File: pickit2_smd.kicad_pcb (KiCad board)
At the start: 2 copper layers, 54 parts, among them CON1 USB-MINI-B, P1 CONN_6, Q1 MOSFET_P, Q2 MOSFET_N, Q3 MOSFET_P, Q4 MOSFET_N, Q5 MOSFET_N, Q6 MOSFET_P, Q7 MOSFET_N, Q8 20MHz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

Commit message: footprint certo pic
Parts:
- U2: footprint SOJ28_WIDE -> SO28
- moved U2 1.40 mm to (190.6, 135.1)
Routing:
- net /RB2: track 108.2 -> 100.5 mm
- net /RB4: track 100.3 -> 93.9 mm
- net /RB5: track 6.89 -> 9.55 mm
- net /RB3: track 39.3 -> 36.6 mm
- net +5V: track 120.6 -> 122.5 mm
- net GND: track 258.2 -> 260.0 mm
- net N-000004: track 31.8 -> 33.4 mm
- net N-000005: track 29.9 -> 31.6 mm
- net /D+: track 11.8 -> 13.1 mm
- net N-0000036: track 16.8 -> 15.9 mm
- net /D-: track 12.6 -> 13.1 mm
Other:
- rule via_min_size: 0.889 -> 1

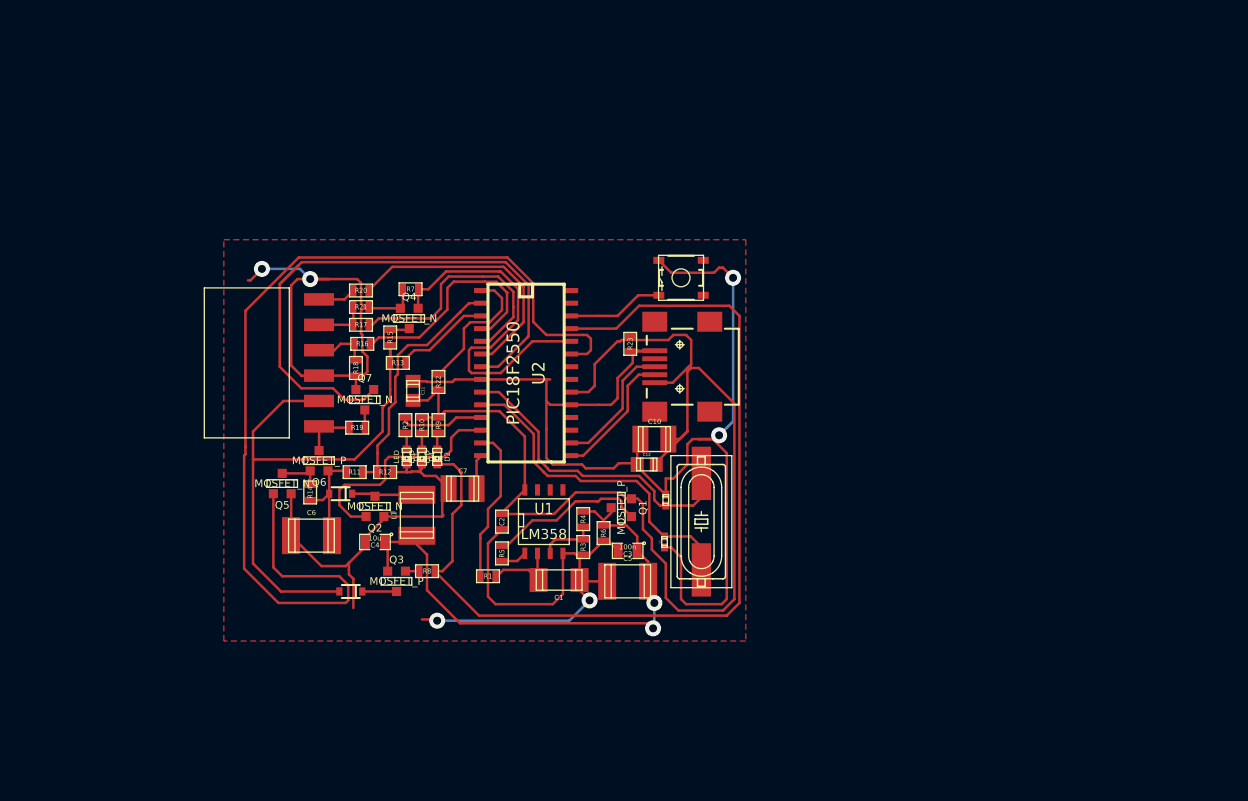
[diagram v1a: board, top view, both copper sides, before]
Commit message: versao modificada, PCB 50%
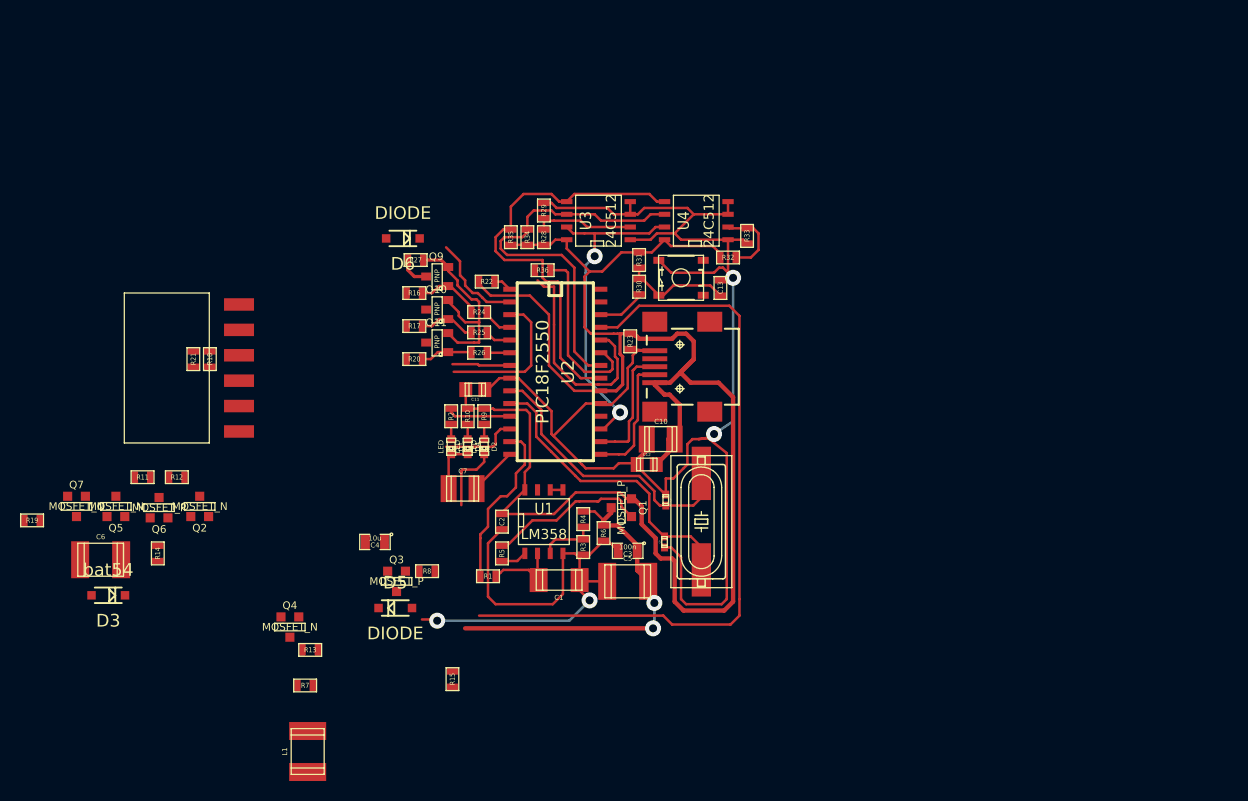
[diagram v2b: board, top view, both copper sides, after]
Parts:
- added C13: 100n, SM0603, F.Cu at (210.1, 126.6)
- added D6: DIODE, SOD123_mod, F.Cu at (178.3, 121.7)
- added Q10: PNP, SOT23, F.Cu at (181.7, 128.8)
- added Q11: PNP, SOT23, F.Cu at (181.7, 132.1)
- added Q9: PNP, SOT23, F.Cu at (181.7, 125.5)
- added R24: 33, SM0603, F.Cu at (185.9, 129.0)
- added R25: 33, SM0603, F.Cu at (185.9, 131.1)
- added R26: 33, SM0603, F.Cu at (185.9, 133.1)
- added R27: 820, SM0603, F.Cu at (179.6, 123.8)
- added R28: R, SM0603, F.Cu at (192.4, 121.5)
- added R29: R, SM0603, F.Cu at (192.4, 118.9)
- added R30: 33, SM0603, F.Cu at (201.9, 126.5)
- added R31: 10k, SM0603, F.Cu at (201.9, 123.8)
- added R32: R, SM0603, F.Cu at (210.8, 123.6)
- added R33: R, SM0603, F.Cu at (212.7, 121.4)
- added R34: R, SM0603, F.Cu at (190.8, 121.5)
- added R35: R, SM0603, F.Cu at (189.1, 121.5)
- added R36: 0, SM0603, F.Cu at (192.3, 124.8)
- added U3: 24C512, SO8N, F.Cu at (197.9, 119.9)
- added U4: 24C512, SO8N, F.Cu at (207.6, 119.9)
- D3: value DIODE -> bat54; footprint SparkFun-SOD-323 -> SOD123_mod
- D5: footprint SparkFun-SOD-323 -> SOD123_mod
- moved R7 41.0 mm to (168.5, 166.4)
- moved R15 34.7 mm to (183.3, 165.7)
- moved R19 33.8 mm to (141.2, 149.9)
- moved Q4 33.1 mm to (167.0, 160.5)
- moved Q7 30.7 mm to (145.7, 148.5)
- moved R13 30.0 mm to (169.0, 162.8)
- moved L1 26.0 mm to (168.8, 173.0)
- moved D3 25.4 mm to (148.8, 157.4)
- moved C6 21.2 mm to (148.1, 153.8)
- moved R11 21.2 mm to (152.3, 145.5)
- moved R12 20.8 mm to (155.7, 145.5)
- moved R21 17.6 mm to (157.4, 133.7), turned to 270 degrees
- moved Q2 17.5 mm to (158.0, 148.5)
- moved Q5 16.8 mm to (149.6, 148.5)
- moved Q6 16.7 mm to (153.9, 148.6)
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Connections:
- R16 pad 1: /RA2 -> N-0000011
- R17 pad 1: /RA3 -> N-0000014
- R20 pad 1: /RA4 -> N-0000017
- SW1 pad 1: /RB5 -> N-0000025
- U1 pad 5: (no net) -> GND
- U1 pad 6: (no net) -> GND
- U1 pad 7: (no net) -> N-0000018
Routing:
- net /RB2: track 100.5 -> 18.0 mm
- net N-0000033: track 55.3 -> 0.00 mm
- net /RA5: track 60.0 -> 5.77 mm
- net +5V: track 122.5 -> 170.5 mm
- net GND: track 260.0 -> 215.8 mm, vias 6 -> 4
- net /RB0: track 0.00 -> 43.5 mm
- net /RB1: track 0.00 -> 39.8 mm
- net /RC6: track 0.00 -> 32.6 mm, vias 0 -> 2
- net /RA4: track 26.4 -> 2.29 mm
- net /RA3: track 25.2 -> 2.60 mm
- net /RA2: track 23.3 -> 3.07 mm
- net /clamp: track 0.00 -> 19.7 mm
- net N-0000048: track 55.3 -> 37.9 mm
- net /RC1: track 23.2 -> 7.68 mm
- net /RB4: track 93.9 -> 78.8 mm
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- removed copper zone on F.Cu, net GND

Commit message: placa feita, falta a bobina e alargar pistas
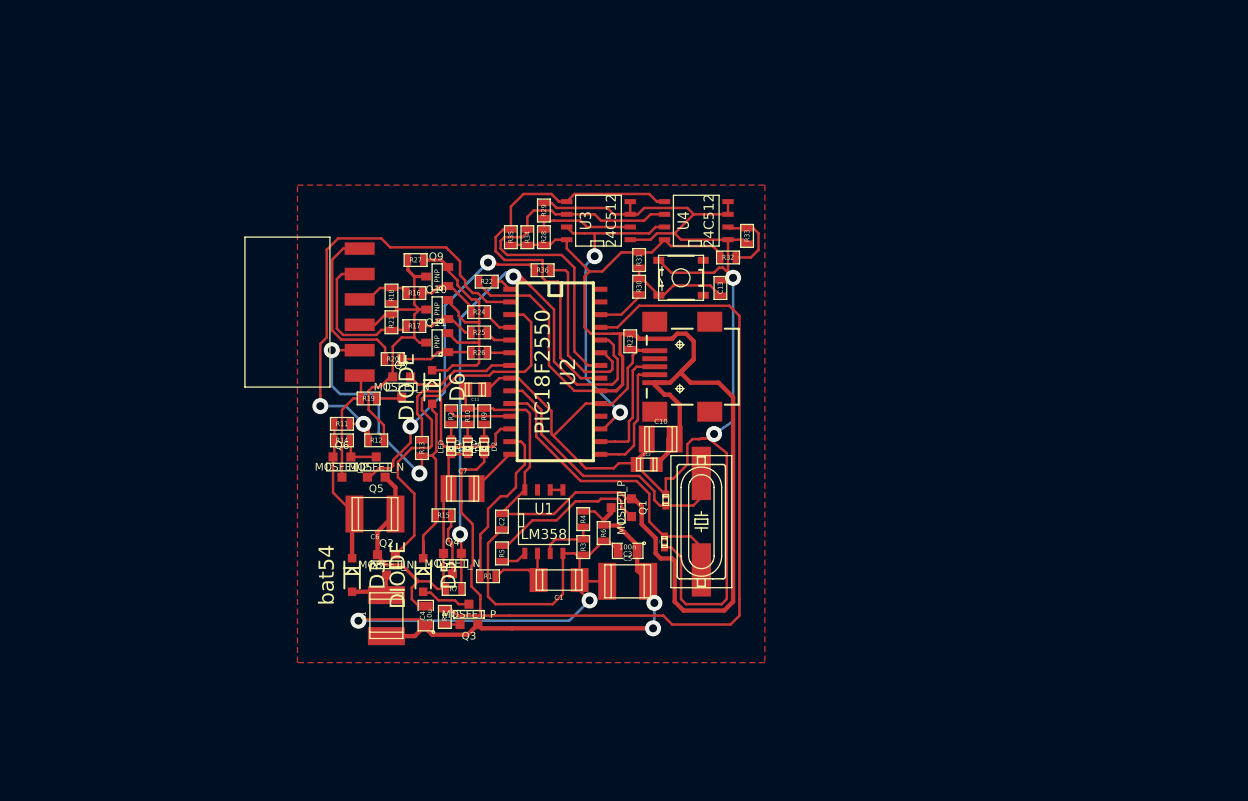
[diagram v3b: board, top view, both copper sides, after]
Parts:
- moved R19 35.8 mm to (174.9, 137.7)
- moved Q7 34.6 mm to (178.2, 136.5)
- moved C6 27.8 mm to (175.5, 149.2), turned to 180 degrees
- moved Q5 26.3 mm to (175.6, 144.5)
- moved D3 24.5 mm to (173.2, 155.3), turned to 270 degrees
- moved R13 23.1 mm to (180.2, 142.6), turned to 90 degrees
- moved R14 21.6 mm to (172.2, 141.9), turned to 0 degrees
- moved R11 20.6 mm to (172.2, 140.2)
- moved R12 20.3 mm to (175.6, 141.9)
- moved R21 20.2 mm to (177.2, 130.0), turned to 90 degrees
- moved Q2 19.6 mm to (176.7, 154.3), turned to 0 degrees
- moved R18 19.2 mm to (177.2, 127.4)
- moved Q6 18.7 mm to (172.2, 144.5), turned to 0 degrees
- moved R7 17.7 mm to (183.4, 156.7)
- moved Q4 17.5 mm to (183.3, 154.2)
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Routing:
- net GND: track 215.8 -> 290.3 mm
- net N-0000033: track 0.00 -> 42.0 mm, vias 0 -> 2
- net /RA0: track 9.73 -> 48.2 mm, vias 0 -> 2
- net /RB3: track 22.0 -> 59.2 mm, vias 0 -> 2
- net /RB2: track 18.0 -> 50.3 mm, vias 0 -> 2
- net /RC1: track 7.68 -> 34.9 mm
- net N-000008: track 0.00 -> 17.8 mm
- net /RB4: track 78.8 -> 94.5 mm
- net N-000007: track 0.00 -> 15.1 mm
- net N-0000060: track 0.00 -> 14.5 mm
- net N-0000029: track 0.00 -> 11.5 mm
- net /RA1: track 14.8 -> 24.2 mm
- net N-0000048: track 37.9 -> 46.9 mm
- net /clamp: track 19.7 -> 26.5 mm
- net N-000009: track 0.00 -> 6.14 mm
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- added copper zone on F.Cu, net GND

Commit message: update
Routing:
- net GND: track 290.3 -> 316.4 mm
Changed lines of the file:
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@@
-(kicad_pcb (version 3) (host pcbnew "(2013-07-07 BZR 4022)-stable")
+(kicad_pcb (version 3) (host pcbnew "(2013-mar-13)-testing")
   (general
     (links 153)
-    (no_connects 3)
+    (no_connects 2)
     (area 161.00888 110.066001 225.168381 164.084001)
     (thickness 1.6)
     (drawings 2)
-    (tracks 728)
+    (tracks 747)
     (zones 0)
     (modules 74)
@@
     (attr smd)
     (fp_text reference U2 (at 0 -1.26492 270) (layer F.SilkS)
-      (effects (font (size 1.524 1.524) (thickness 0.1524)))
+      (effects (font (thickness 0.1524)))
     )
     (fp_text value PIC18F2550 (at 0 1.27 270) (layer F.SilkS)
-      (effects (font (size 1.524 1.524) (thickness 0.1524)))
+      (effects (font (thickness 0.1524)))
     )
     (fp_line (start 8.89 -2.54) (end 8.89 3.81) (layer F.SilkS) (width 0.3048))
@@
     (at 173.228 155.321 270)
     (fp_text reference D3 (at 0 -2.54 270) (layer F.SilkS)
-      (effects (font (size 1.524 1.524) (thickness 0.3048)))
+      (effects (font (thickness 0.3048)))
     )
     (fp_text value bat54 (at 0 2.54 270) (layer F.SilkS)
-      (effects (font (size 1.524 1.524) (thickness 0.3048)))
+      (effects (font (thickness 0.3048)))
     )
     (fp_line (start 1.34874 0.7747) (end -1.34874 0.7747) (layer F.SilkS) (width 0.1905))
@@
     (at 180.34 155.321 270)
     (fp_text reference D5 (at 0 -2.54 270) (layer F.SilkS)
-      (effects (font (size 1.524 1.524) (thickness 0.3048)))
+      (effects (font (thickness 0.3048)))
     )
     (fp_text value DIODE (at 0 2.54 270) (layer F.SilkS)
-      (effects (font (size 1.524 1.524) (thickness 0.3048)))
+      (effects (font (thickness 0.3048)))
     )
     (fp_line (start 1.34874 0.7747) (end -1.34874 0.7747) (layer F.SilkS) (width 0.1905))
@@
     (at 181.229 136.525 270)
     (fp_text reference D6 (at 0 -2.54 270) (layer F.SilkS)
-      (effects (font (size 1.524 1.524) (thickness 0.3048)))
+      (effects (font (thickness 0.3048)))
     )
     (fp_text value DIODE (at 0 2.54 270) (layer F.SilkS)
-      (effects (font (size 1.524 1.524) (thickness 0.3048)))
+      (effects (font (thickness 0.3048)))
     )
     (fp_line (start 1.34874 0.7747) (end -1.34874 0.7747) (layer F.SilkS) (width 0.1905))
@@
   (segment (start 201.93 135.29056) (end 203.49464 135.29056) (width 0.254) (layer F.Cu) (net 3))
   (segment (start 198.12 143.256) (end 199.898 143.256) (width 0.254) (layer F.Cu) (net 3))
-  (segment (start 174.879 141.859) (end 174.879 140.716) (width 0.254) (layer F.Cu) (net 4) (status 400000))
+  (segment (start 177.038 122.555) (end 176.4665 122.555) (width 0.254) (layer F.Cu) (net 4))
+  (segment (start 175.5775 121.666) (end 175.26 121.666) (width 0.254) (layer F.Cu) (net 4))
+  (segment (start 176.4665 122.555) (end 175.5775 121.666) (width 0.254) (layer F.Cu) (net 4))
+  (segment (start 174.879 141.859) (end 174.879 140.716) (width 0.254) (layer F.Cu) (net 4))
   (segment (start 170.053 138.43) (end 170.053 137.414) (width 0.254) (layer F.Cu) (net 4))
   (via (at 170.053 138.43) (size 1.6) (layers F.Cu B.Cu) (net 4))
@@
   (segment (start 174.879 140.716) (end 174.371 140.208) (width 0.254) (layer F.Cu) (net 4))
   (segment (start 182.626 122.555) (end 177.038 122.555) (width 0.254) (layer F.Cu) (net 4))
-  (segment (start 177.038 122.555) (end 176.149 121.666) (width 0.254) (layer F.Cu) (net 4))
-  (segment (start 176.149 121.666) (end 171.831 121.666) (width 0.254) (layer F.Cu) (net 4))
+  (segment (start 175.26 121.666) (end 171.831 121.666) (width 0.254) (layer F.Cu) (net 4))
   (segment (start 171.831 121.666) (end 170.688 122.809) (width 0.254) (layer F.Cu) (net 4))
   (segment (start 170.688 122.809) (end 170.688 131.572) (width 0.254) (layer F.Cu) (net 4))
@@
   (segment (start 198.12 119.888) (end 202.438 119.888) (width 0.254) (layer F.Cu) (net 11))
   (segment (start 186.817 124.079) (end 187.579 124.079) (width 0.254) (layer F.Cu) (net 12))
-  (segment (start 175.006 145.542) (end 175.895 144.653) (width 0.254) (layer F.Cu) (net 12) (status 400000))
+  (segment (start 175.006 145.542) (end 175.895 144.653) (width 0.254) (layer F.Cu) (net 12))
   (segment (start 175.895 144.653) (end 177.081998 144.653) (width 0.254) (layer F.Cu) (net 12))
   (segment (start 177.081998 144.653) (end 177.335998 144.399) (width 0.254) (layer F.Cu) (net 12))
@@
   (segment (start 182.499 128.397) (end 186.817 124.079) (width 0.254) (layer B.Cu) (net 12))
   (via (at 186.817 124.079) (size 1.6) (layers F.Cu B.Cu) (net 12))
-  (segment (start 174.752 145.542) (end 175.006 145.542) (width 0.254) (layer F.Cu) (net 12) (status C00000))
-  (segment (start 190.964002 124.289002) (end 191.516 124.841) (width 0.254) (layer F.Cu) (net 12) (status 800000))
+  (segment (start 174.752 145.542) (end 175.006 145.542) (width 0.254) (layer F.Cu) (net 12))
+  (segment (start 190.964002 124.289002) (end 191.516 124.841) (width 0.254) (layer F.Cu) (net 12))
   (segment (start 187.789002 124.289002) (end 190.964002 124.289002) (width 0.254) (layer F.Cu) (net 12))
   (segment (start 187.579 124.079) (end 187.789002 124.289002) (width 0.254) (layer F.Cu) (net 12))
@@
   (segment (start 183.896 129.032) (end 183.896 129.413) (width 0.254) (layer F.Cu) (net 23))
   (segment (start 182.83682 127.97282) (end 183.896 129.032) (width 0.254) (layer F.Cu) (net 23))
-  (segment (start 177.292 135.509) (end 177.038 135.509) (width 0.254) (layer F.Cu) (net 24) (status C00000))
-  (segment (start 176.403 140.335) (end 176.403 141.859) (width 0.254) (layer F.Cu) (net 24) (status 800000))
+  (segment (start 194.31 153.162) (end 194.31 153.67) (width 0.254) (layer F.Cu) (net 24) (status C00000))
+  (segment (start 198.247 151.892) (end 198.374 151.892) (width 0.254) (layer F.Cu) (net 24) (status C00000))
+  (segment (start 197.358 151.003) (end 198.247 151.892) (width 0.254) (layer F.Cu) (net 24) (status 800000))
+  (segment (start 197.358 149.9235) (end 197.358 151.003) (width 0.254) (layer F.Cu) (net 24))
+  (segment (start 197.1675 149.733) (end 197.358 149.9235) (width 0.254) (layer F.Cu) (net 24))
+  (segment (start 194.691 149.733) (end 197.1675 149.733) (width 0.254) (layer F.Cu) (net 24))
+  (segment (start 192.405 152.019) (end 194.691 149.733) (width 0.254) (layer F.Cu) (net 24))
+  (segment (start 192.405 154.1145) (end 192.405 152.019) (width 0.254) (layer F.Cu) (net 24))
+  (segment (start 192.4685 154.178) (end 192.405 154.1145) (width 0.254) (layer F.Cu) (net 24))
+  (segment (start 193.802 154.178) (end 192.4685 154.178) (width 0.254) (layer F.Cu) (net 24))
+  (segment (start 194.31 153.67) (end 193.802 154.178) (width 0.254) (layer F.Cu) (net 24) (status 400000))
+  (segment (start 169.8625 140.335) (end 171.7675 138.43) (width 0.254) (layer F.Cu) (net 24))
+  (segment (start 176.784 135.509) (end 177.292 135.509) (width 0.254) (layer F.Cu) (net 24) (status 800000))
+  (segment (start 175.387 134.112) (end 176.784 135.509) (width 0.254) (layer F.Cu) (net 24))
+  (segment (start 172.1485 134.112) (end 175.387 134.112) (width 0.254) (layer F.Cu) (net 24))
+  (segment (start 171.7675 134.493) (end 172.1485 134.112) (width 0.254) (layer F.Cu) (net 24))
+  (segment (start 171.7675 138.43) (end 171.7675 134.493) (width 0.254) (layer F.Cu) (net 24))
+  (segment (start 177.292 135.509) (end 177.038 135.509) (width 0.254) (layer F.Cu) (net 24))
+  (segment (start 176.403 140.335) (end 176.403 141.859) (width 0.254) (layer F.Cu) (net 24))
   (segment (start 174.879 138.811) (end 176.403 140.335) (width 0.254) (layer F.Cu) (net 24))
   (segment (start 174.879 136.906) (end 174.879 138.811) (width 0.254) (layer F.Cu) (net 24))
   (segment (start 175.26 136.525) (end 174.879 136.906) (width 0.254) (layer F.Cu) (net 24))
   (segment (start 176.022 136.525) (end 175.26 136.525) (width 0.254) (layer F.Cu) (net 24))
-  (segment (start 177.038 135.509) (end 176.022 136.525) (width 0.254) (layer F.Cu) (net 24) (status 400000))
-  (segment (start 177.292 135.509) (end 177.292 132.461) (width 0.254) (layer F.Cu) (net 24) (status 400000))
+  (segment (start 177.038 135.509) (end 176.022 136.525) (width 0.254) (layer F.Cu) (net 24))
+  (segment (start 177.292 135.509) (end 177.292 132.461) (width 0.254) (layer F.Cu) (net 24))
   (segment (start 178.181 131.572) (end 179.451 131.572) (width 0.254) (layer F.Cu) (net 24))
   (segment (start 177.292 132.461) (end 178.181 131.572) (width 0.254) (layer F.Cu) (net 24))
@@
   (segment (start 177.165 130.81) (end 178.308 130.81) (width 0.254) (layer F.Cu) (net 54))
   (segment (start 178.308 130.81) (end 178.689 130.429) (width 0.254) (layer F.Cu) (net 54))
-  (segment (start 176.53 133.731) (end 176.53 132.588) (width 0.254) (layer F.Cu) (net 55) (status 400000))
+  (segment (start 176.53 133.731) (end 176.53 132.588) (width 0.254) (layer F.Cu) (net 55))
   (segment (start 172.146804 131.782002) (end 171.239998 130.875196) (width 0.254) (layer F.Cu) (net 55))
   (segment (start 171.239998 130.875196) (end 171.239998 123.781002) (width 0.254) (layer F.Cu) (net 55))

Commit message: placa feita
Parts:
- added R37: 0, SM0603, F.Cu at (177.3, 122.6)
- added R38: 0, SM0603, F.Cu at (189.1, 119.4)
- added R39: 0, SM0603, F.Cu at (202.8, 132.0)
- added R40: 0, SM0603, F.Cu at (197.4, 161.4)
- added R41: 0, SM0603, F.Cu at (203.3, 159.4)
- added R42: 0, SM0603, F.Cu at (192.8, 159.4)
- C4: value 10u -> 100n
- C5: value 100n -> 10u
- C7: value CAPAPOL -> 22p; footprint c_1210 -> SM0805
- L1: footprint c_1812 -> inductor_SDE6603
- moved R12 20.7 mm to (183.1, 122.6), turned to 90 degrees
- moved L1 4.28 mm to (172.5, 160.3), turned to 0 degrees
- moved C7 3.89 mm to (188.1, 145.9), turned to 270 degrees
- moved CON1 2.03 mm to (208.0, 134.5)
- moved R11 1.63 mm to (170.9, 139.2), turned to 135 degrees
- moved C4 1.17 mm to (180.3, 160.5)
- moved Q1 0.38 mm to (199.8, 148.6)
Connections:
- C3 pad 1: N-0000048 -> N-0000044
- C4 pad 1: N-0000048 -> N-000007
- C5 pad 1: N-0000048 -> N-0000044
- L1 pad 2: N-0000048 -> N-000007
- Q1 pad D: N-0000048 -> N-0000044
- Q3 pad S: N-0000048 -> N-000007
- R4 pad 2: N-0000048 -> N-0000044
- R6 pad 1: N-0000048 -> N-0000044
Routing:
- net GND: track 316.4 -> 393.1 mm, vias 4 -> 0
- net N-0000048: track 46.9 -> 0.00 mm, vias 2 -> 0
- net N-000007: track 0.00 -> 27.6 mm
- net N-0000044: track 0.00 -> 17.6 mm
- net /RA0: track 48.2 -> 39.0 mm, vias 2 -> 0
- net N-0000022: track 4.80 -> 2.08 mm
- net N-0000023: track 5.58 -> 7.72 mm
- net N-0000025: track 42.0 -> 43.3 mm
- net /RC2: track 17.0 -> 18.1 mm
- net /RB2: track 50.3 -> 49.5 mm
- net /D-: track 12.5 -> 13.4 mm
- net +5V: track 170.5 -> 169.7 mm
- net /D+: track 12.3 -> 13.0 mm
- net /RB0: track 43.5 -> 42.9 mm
- net /RB1: track 39.8 -> 39.2 mm

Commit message: feito, shunt
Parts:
- added R43: 10K, SM0603, F.Cu at (201.0, 129.5)
- C7: value 22p -> 470n
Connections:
- CON1 pad 4: N-0000059 -> (no net)
- U1 pad 7: N-0000047 -> (no net)
- U2 pad 18: /RC7 -> (no net)
- U2 pad 27: /RB6 -> (no net)
- U2 pad 28: /RB7 -> (no net)
